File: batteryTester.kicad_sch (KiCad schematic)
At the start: 41 parts, among them J1 OLED_DISPLAY, J2 USB_C_Receptacle_USB2.0_16P, J3 PROG, Q1 IRF540N, SW1 START, SW2 STOP, SW3 STOP, U1 AMS1117-3.3, U2 LMV321, U3 LMV321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

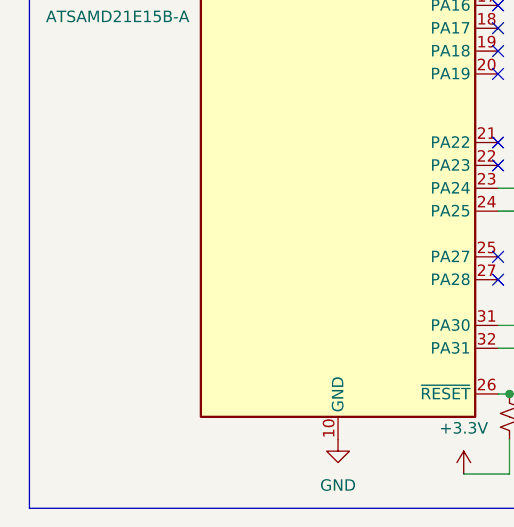
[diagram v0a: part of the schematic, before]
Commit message: add i2c pullups
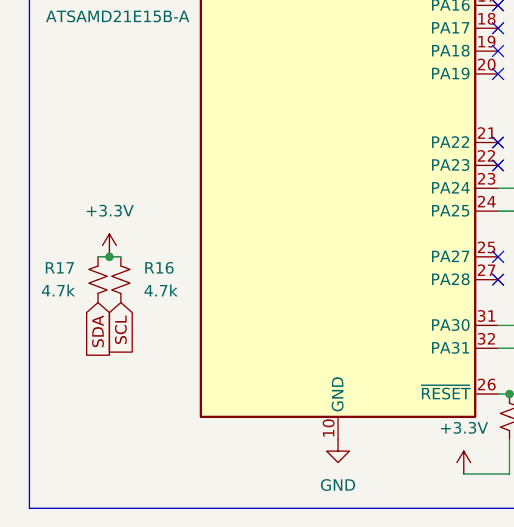
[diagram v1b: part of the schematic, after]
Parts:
- added R16, R17: 4.7k, Resistor_SMD:R_0402_1005Metric, symbol Device:R_Small_US
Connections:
- net +3.3V: now also R16.1, R17.1
- net SCL: now also R16.2
- net SDA: now also R17.2
